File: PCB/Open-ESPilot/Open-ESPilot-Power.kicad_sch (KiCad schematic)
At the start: 33 parts, among them J2 VOUT, J3 VIN, J4 GND, M1 Clone "MP1584" module, Q1 AO3401A, U2 AMS1117-3.3, U3 AMS1117-3.3, U4 INA219AxD

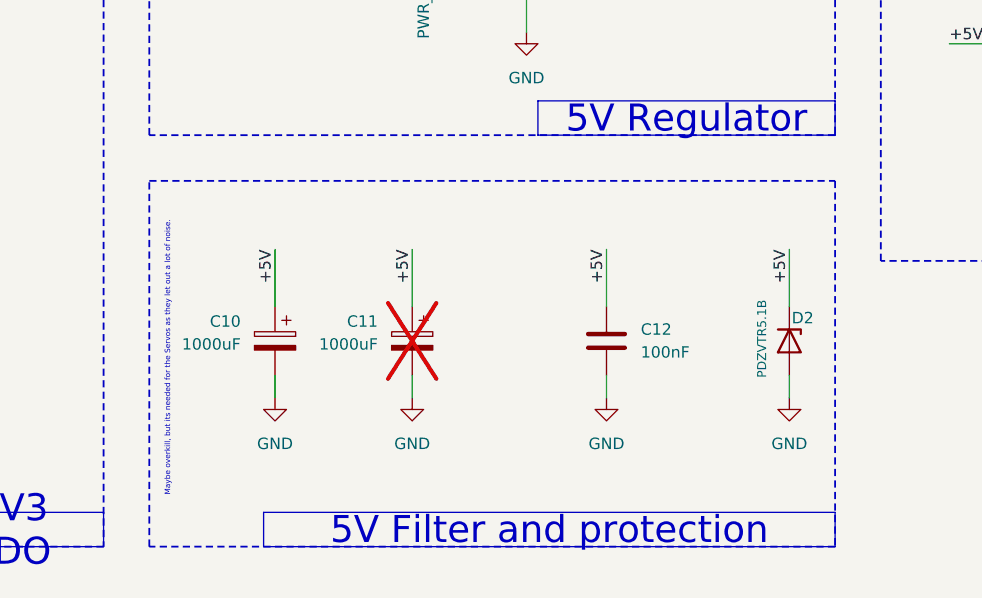
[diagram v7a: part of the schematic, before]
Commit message: halve of the PCB is routed.
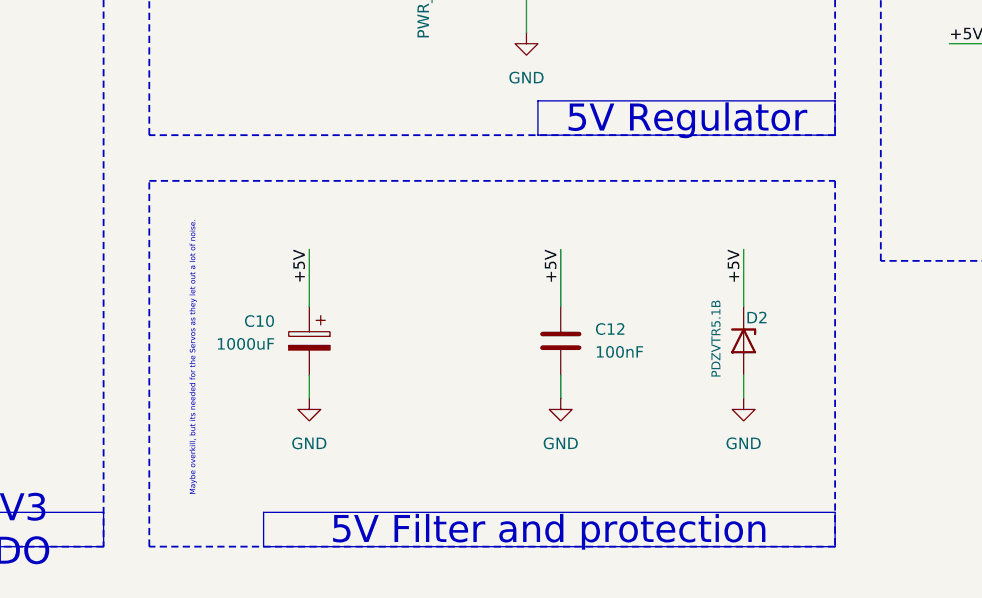
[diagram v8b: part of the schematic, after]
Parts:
- removed C11: 1000uF, Capacitor_THT:CP_Radial_D10.0mm_P5.00mm_P7.50mm, symbol Device:C_Polarized
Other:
- moved on the sheet: C10, C12, D2
